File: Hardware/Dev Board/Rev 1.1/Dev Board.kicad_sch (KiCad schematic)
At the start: 40 parts, among them J1 VBAT, J2 RJ45_LED, J3 GPIO, J4 Ethernet, J5 USB_C_Receptacle_USB2.0, J6 6502 Bus, J7 USB Host, J8 Panel, J9 Serial, SW1 Run/Stop, SW2 Step, SW3 Clock, SW4 Reset, U1 TXS0108EPW, U2 TXS0108EPW, U3 Teensy4.1, U4 TXS0108EPW, U5 TXS0108EPW

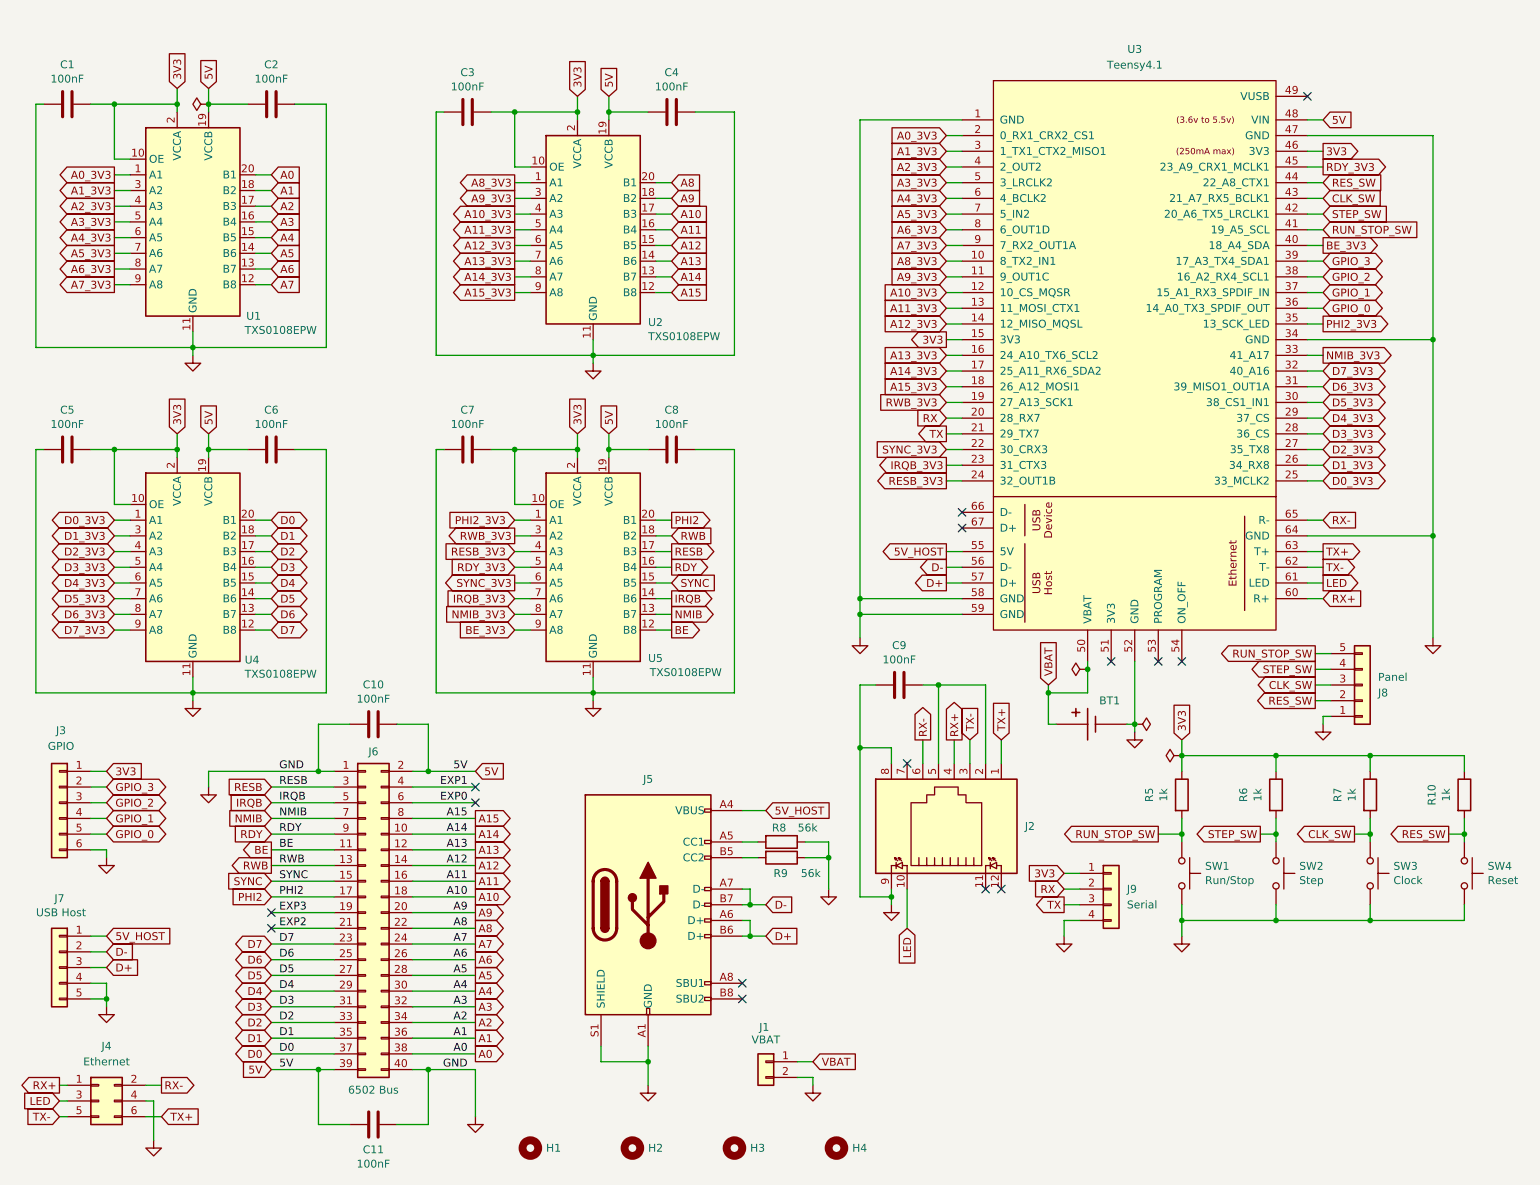
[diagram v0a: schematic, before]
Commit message: Update DB 1.1 to add OE control lines
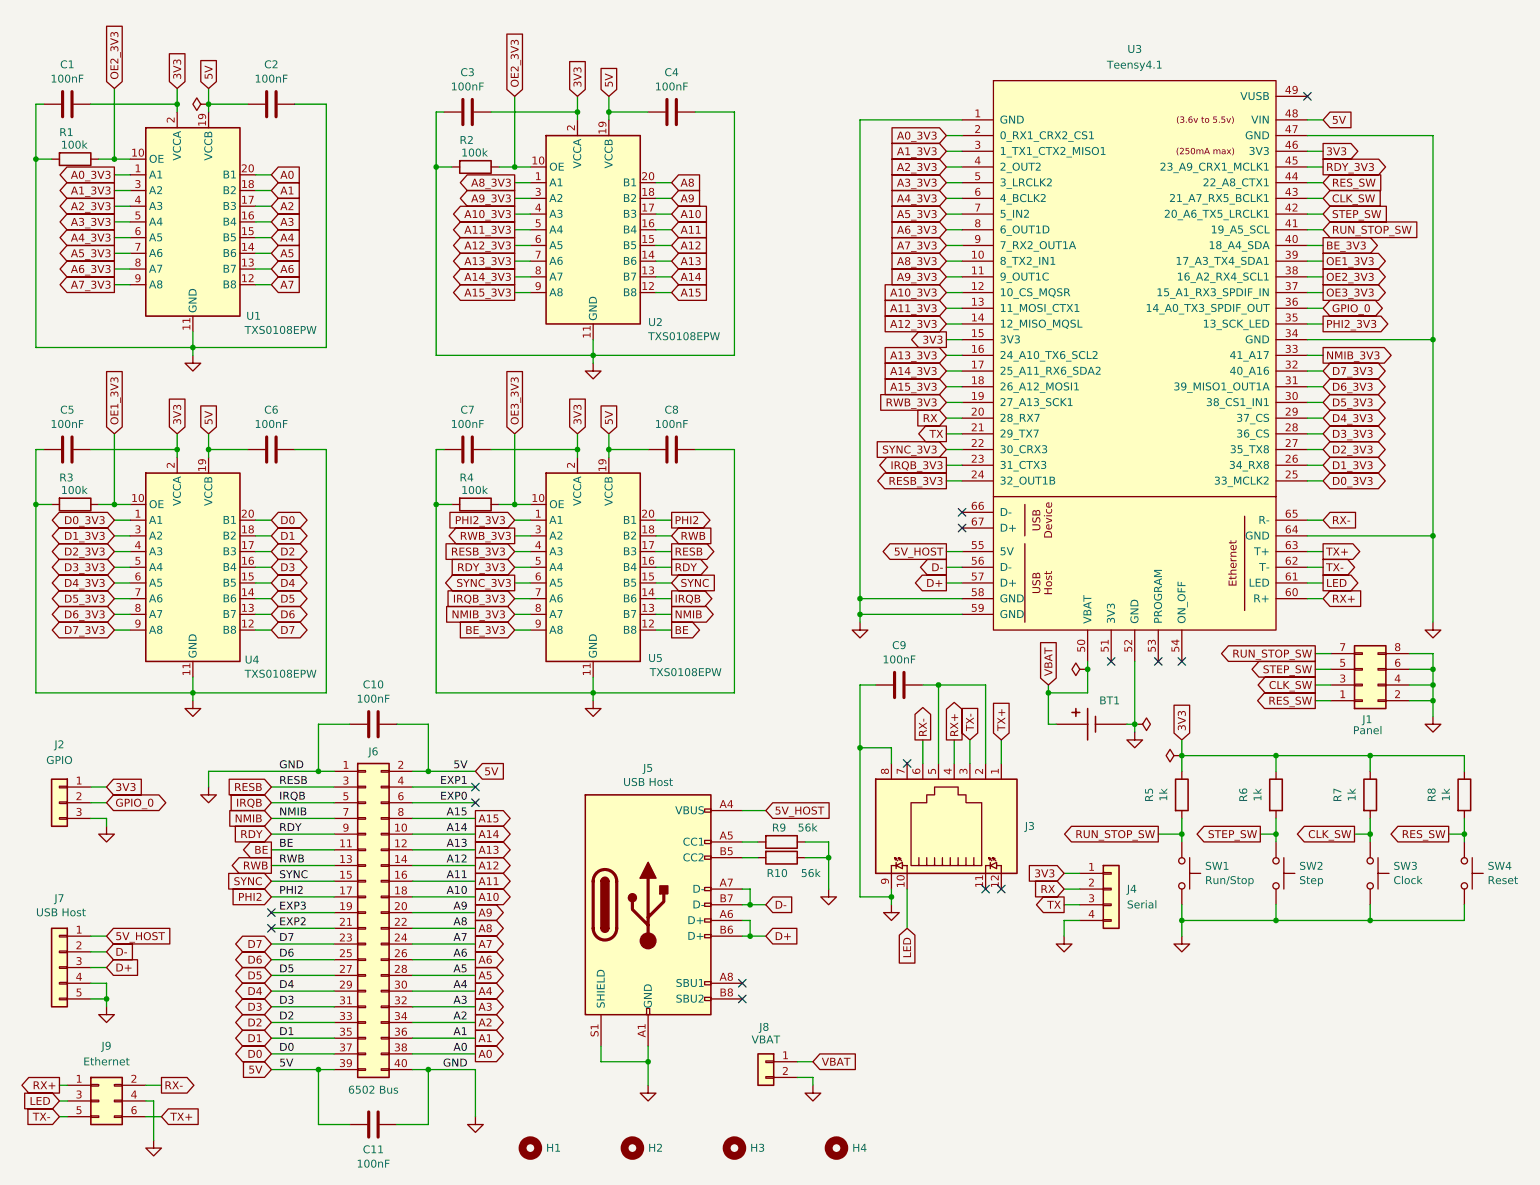
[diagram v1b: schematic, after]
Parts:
- added R1, R2, R3, R4: 100k, Resistor_SMD:R_0805_2012Metric, symbol Device:R
- J1: renamed from J8; footprint Connector_JST:JST_XH_B5B-XH-A_1x05_P2.50mm_Vertical -> Connector_PinHeader_2.54mm:PinHeader_2x04_P2.54mm_Vertical; symbol Connector_Generic:Conn_01x05 -> Connector_Generic:Conn_02x04_Odd_Even; now in the parts list
- J2: renamed from J3; footprint Connector_PinHeader_2.54mm:PinHeader_1x06_P2.54mm_Horizontal -> Connector_PinHeader_2.54mm:PinHeader_1x03_P2.54mm_Horizontal; symbol Connector_Generic:Conn_01x06 -> Connector_Generic:Conn_01x03; now in the parts list
- J5: value USB_C_Receptacle_USB2.0 -> USB Host
- renumbered J2 to J3, J9 to J4, J1 to J8, J4 to J9, R9 to R10, R10 to R8, R8 to R9
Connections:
- net 3V3: no longer U1.10 (OE), U2.10 (OE), U4.10 (OE), U5.10 (OE)
- net GND: now also J1.2 (Pin_2), J1.4 (Pin_4), J1.6 (Pin_6), J1.8 (Pin_8), J2.3 (Pin_3), R1.2, R2.2, R3.2, R4.2; no longer J1.1 (Pin_1), J2.6 (Pin_6)
- net GPIO_0: now also J2.2 (Pin_2); no longer J2.5 (Pin_5)
- net RES_SW: now also J1.1 (Pin_1); no longer J1.2 (Pin_2)
- net RUN_STOP_SW: now also J1.7 (Pin_7); no longer J1.5 (Pin_5)
- net STEP_SW: now also J1.5 (Pin_5); no longer J1.4 (Pin_4)
- net GPIO_1 renamed OE3_3V3
- net OE3_3V3: now also U5.10 (OE), R4.1; no longer J2.4 (Pin_4)
- net GPIO_2 renamed OE2_3V3
- net OE2_3V3: now also U1.10 (OE), U2.10 (OE), R1.1, R2.1; no longer J2.3 (Pin_3)
- net GPIO_3 renamed OE1_3V3
- net OE1_3V3: now also U4.10 (OE), R3.1; no longer J2.2 (Pin_2)
